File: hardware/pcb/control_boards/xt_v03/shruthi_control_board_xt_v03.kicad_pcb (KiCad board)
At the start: 2 copper layers, 286 x 99.4 mm, 127 parts, among them IC1 24LC512, IC10 ATMEGA644p, IC2 74HC165N, IC3 74HC165N, IC4 4051, IC5 4051, IC6 4051, IC7 4051, IC8 74595N, IC9 74HC165N, J1 Conn_01x08, J2 Conn_01x06, Q1 20MHz, SW1 Encoder, U1 AVRISP, X1 MIDI, X2 MIDI

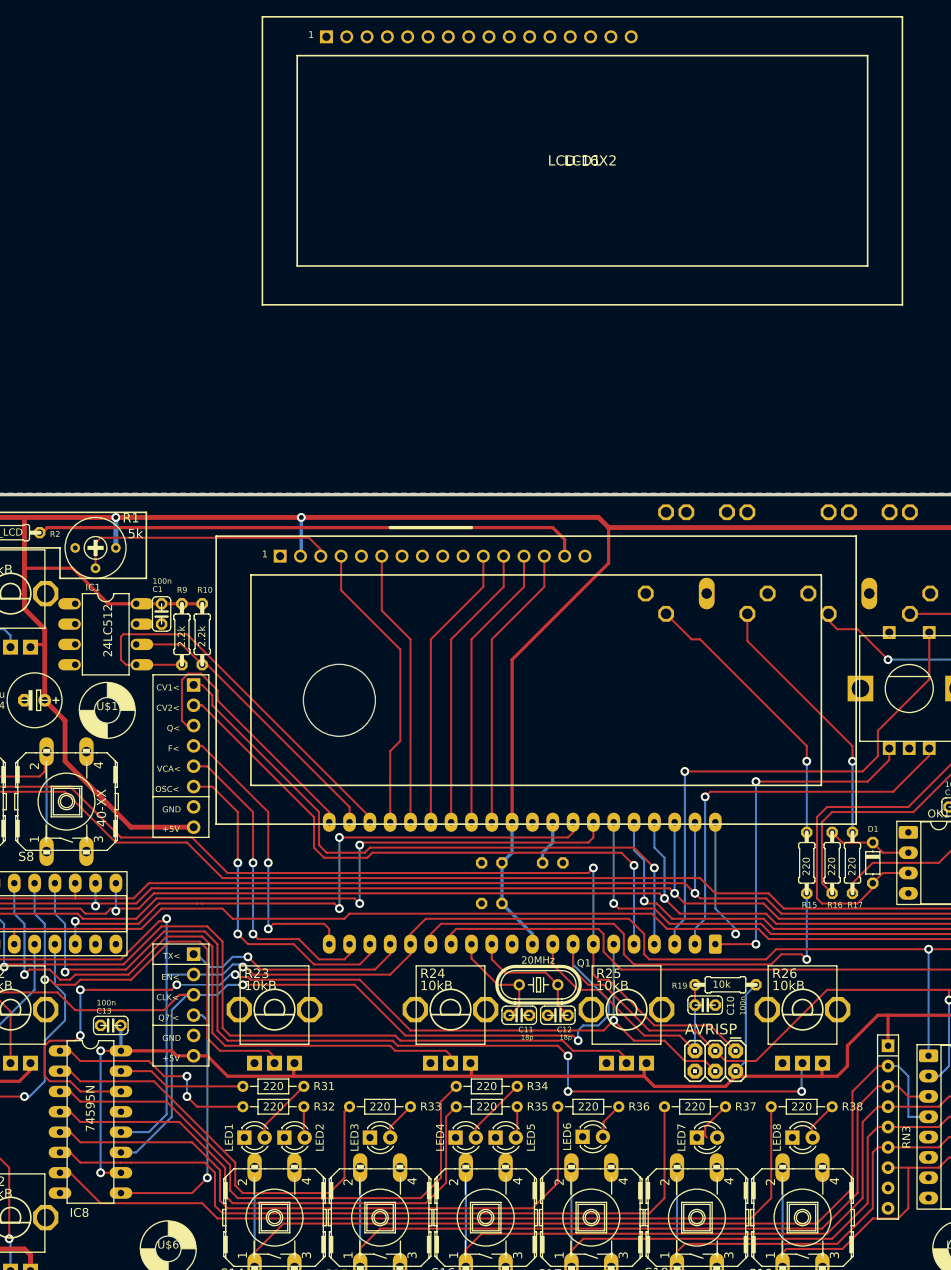
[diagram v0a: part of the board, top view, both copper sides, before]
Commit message: update footprint for 74HC595
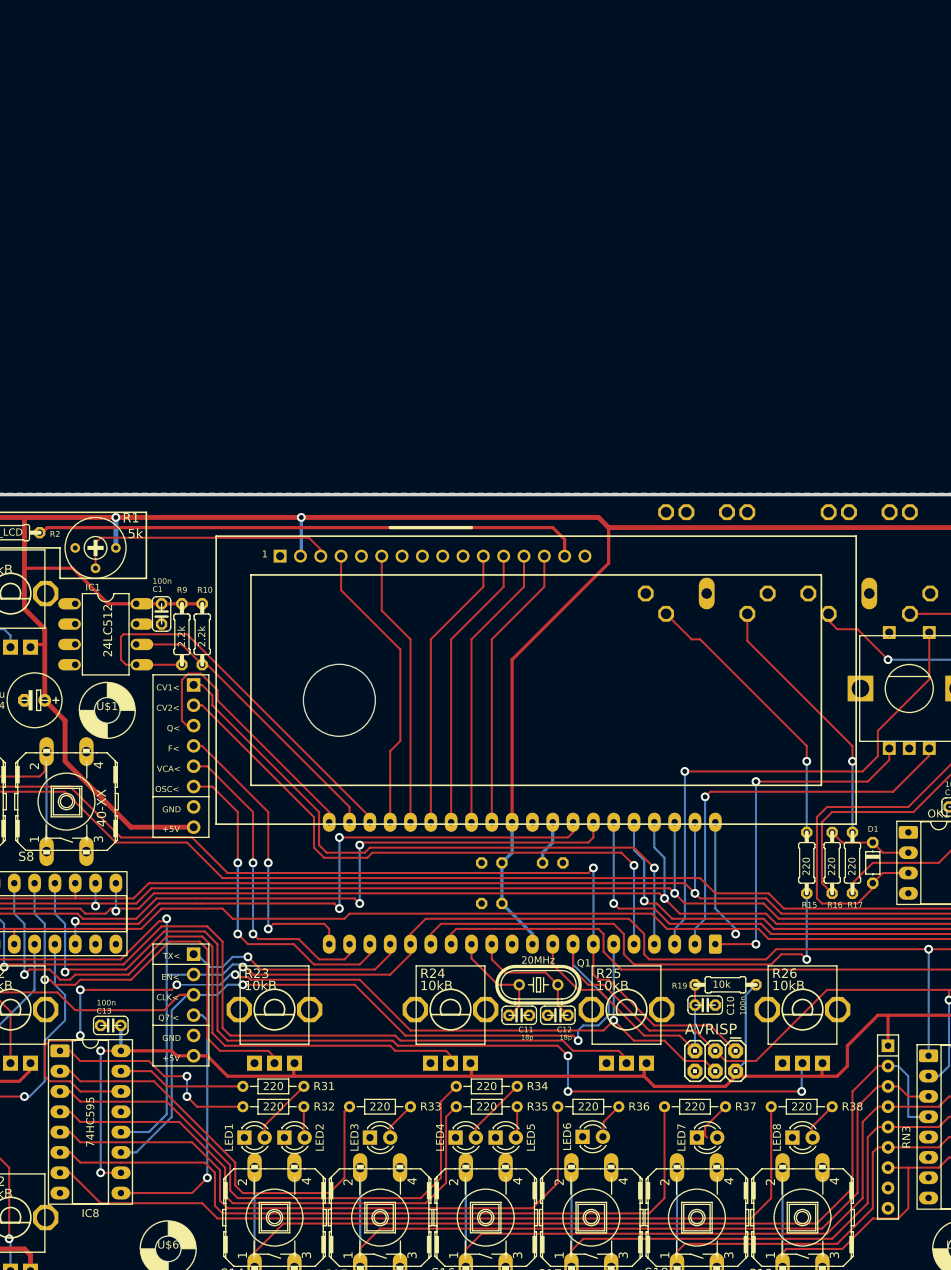
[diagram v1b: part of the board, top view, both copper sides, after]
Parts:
- removed LCD1: LCD-16X2, shruthi_control_board_xt_v03:LCD-16X2
- IC8: value 74595N -> 74HC595; footprint shruthi_control_board_xt_v03:DIL16 -> Package_DIP:DIP-16_W7.62mm_Socket_LongPads
- moved IC8 9.67 mm to (154.1, 163.2), turned to 0 degrees

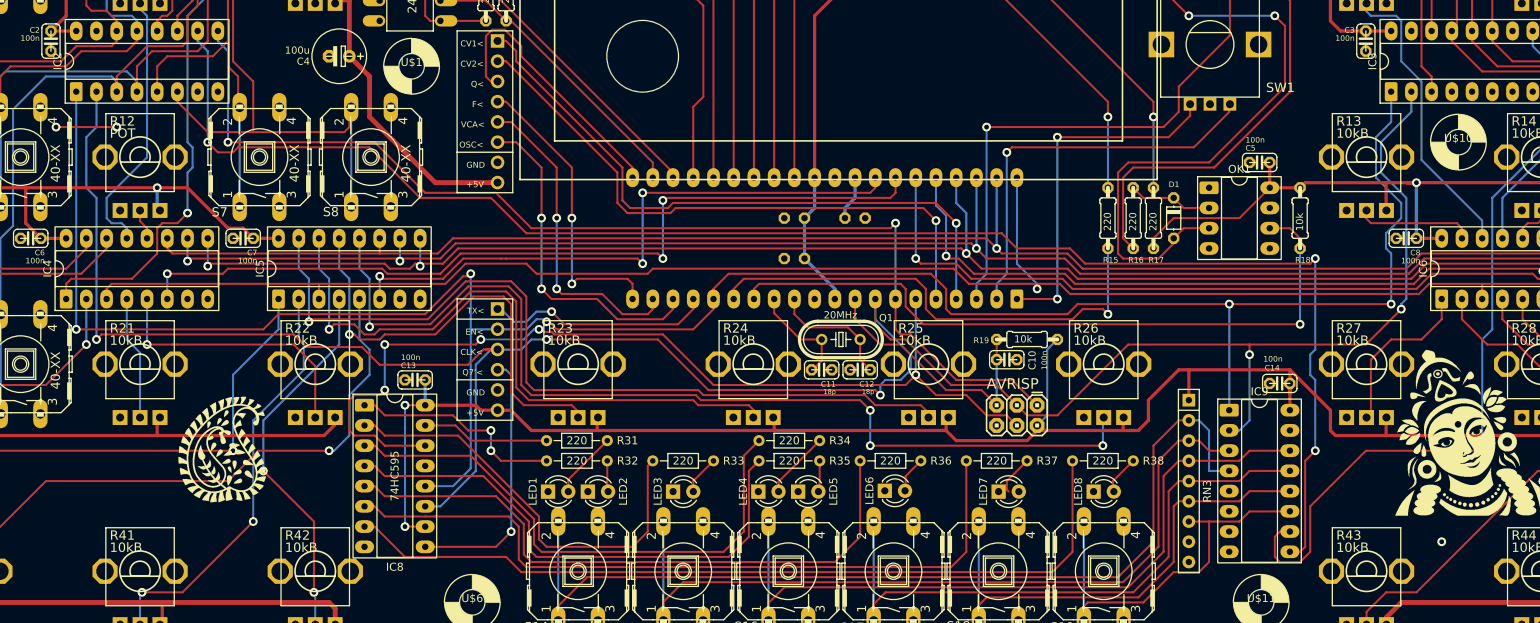
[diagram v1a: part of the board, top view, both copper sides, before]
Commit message: update silkscreen for 74HC165s
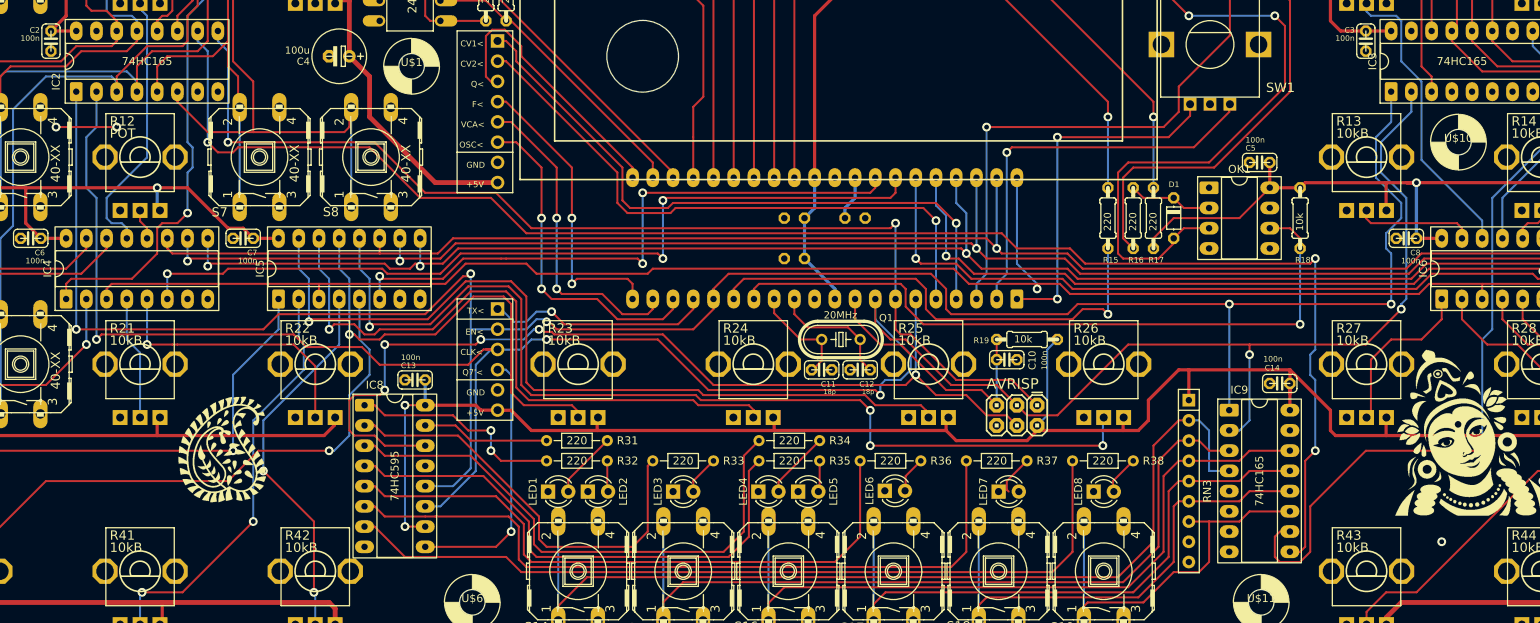
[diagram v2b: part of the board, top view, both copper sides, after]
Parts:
- IC2, IC3, IC9: value 74HC165N -> 74HC165
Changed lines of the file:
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@@
 			)
 		)
-		(property "Value" "74HC165N"
-			(at 3.81 20.11 90)
-			(layer "F.Fab")
+		(property "Value" "74HC165"
+			(at 3.81 8.89 180)
+			(layer "F.SilkS")
 			(effects
 				(font
@@
 		(tags "THT DIP DIL PDIP 2.54mm 7.62mm 300mil Socket LongPads")
 		(property "Reference" "IC8"
-			(at 3.81 20.32 0)
+			(at 1.27 -2.54 0)
 			(layer "F.SilkS")
 			(effects
@@
 		(tags "THT DIP DIL PDIP 2.54mm 7.62mm 300mil Socket LongPads")
 		(property "Reference" "IC9"
-			(at 3.81 -2.33 0)
+			(at 1.27 -2.54 0)
 			(layer "F.SilkS")
 			(effects
@@
 			)
 		)
-		(property "Value" "74HC165N"
-			(at 3.81 20.11 0)
-			(layer "F.Fab")
+		(property "Value" "74HC165"
+			(at 3.81 8.89 90)
+			(layer "F.SilkS")
 			(effects
 				(font
@@
 		(tags "THT DIP DIL PDIP 2.54mm 7.62mm 300mil Socket LongPads")
 		(property "Reference" "IC2"
-			(at 3.81 -2.33 90)
+			(at 1.27 -2.54 90)
 			(layer "F.SilkS")
 			(effects
@@
 			)
 		)
-		(property "Value" "74HC165N"
-			(at 3.81 20.11 90)
-			(layer "F.Fab")
+		(property "Value" "74HC165"
+			(at 3.81 8.89 180)
+			(layer "F.SilkS")
 			(effects
 				(font
